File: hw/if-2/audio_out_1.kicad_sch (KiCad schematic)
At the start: 0 parts

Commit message: First draft of schematic
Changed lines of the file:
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@@
 	(text "(Will Be Copy of R1 Audio Output)"
 		(exclude_from_sim no)
-		(at 141.732 90.932 0)
+		(at 146.812 103.124 0)
 		(effects
 			(font

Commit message: First draft of schematic
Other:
- note added: "(Will Be Copy of R0 Audio Output)"
- note removed: "(Will Be Copy of R1 Audio Output)"
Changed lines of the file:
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@@
 		(comment 2 "NOT FOR COMMERCIAL USE")
 	)
-	(text "(Will Be Copy of R1 Audio Output)"
+	(text "(Will Be Copy of R0 Audio Output)"
 		(exclude_from_sim no)
 		(at 146.812 103.124 0)

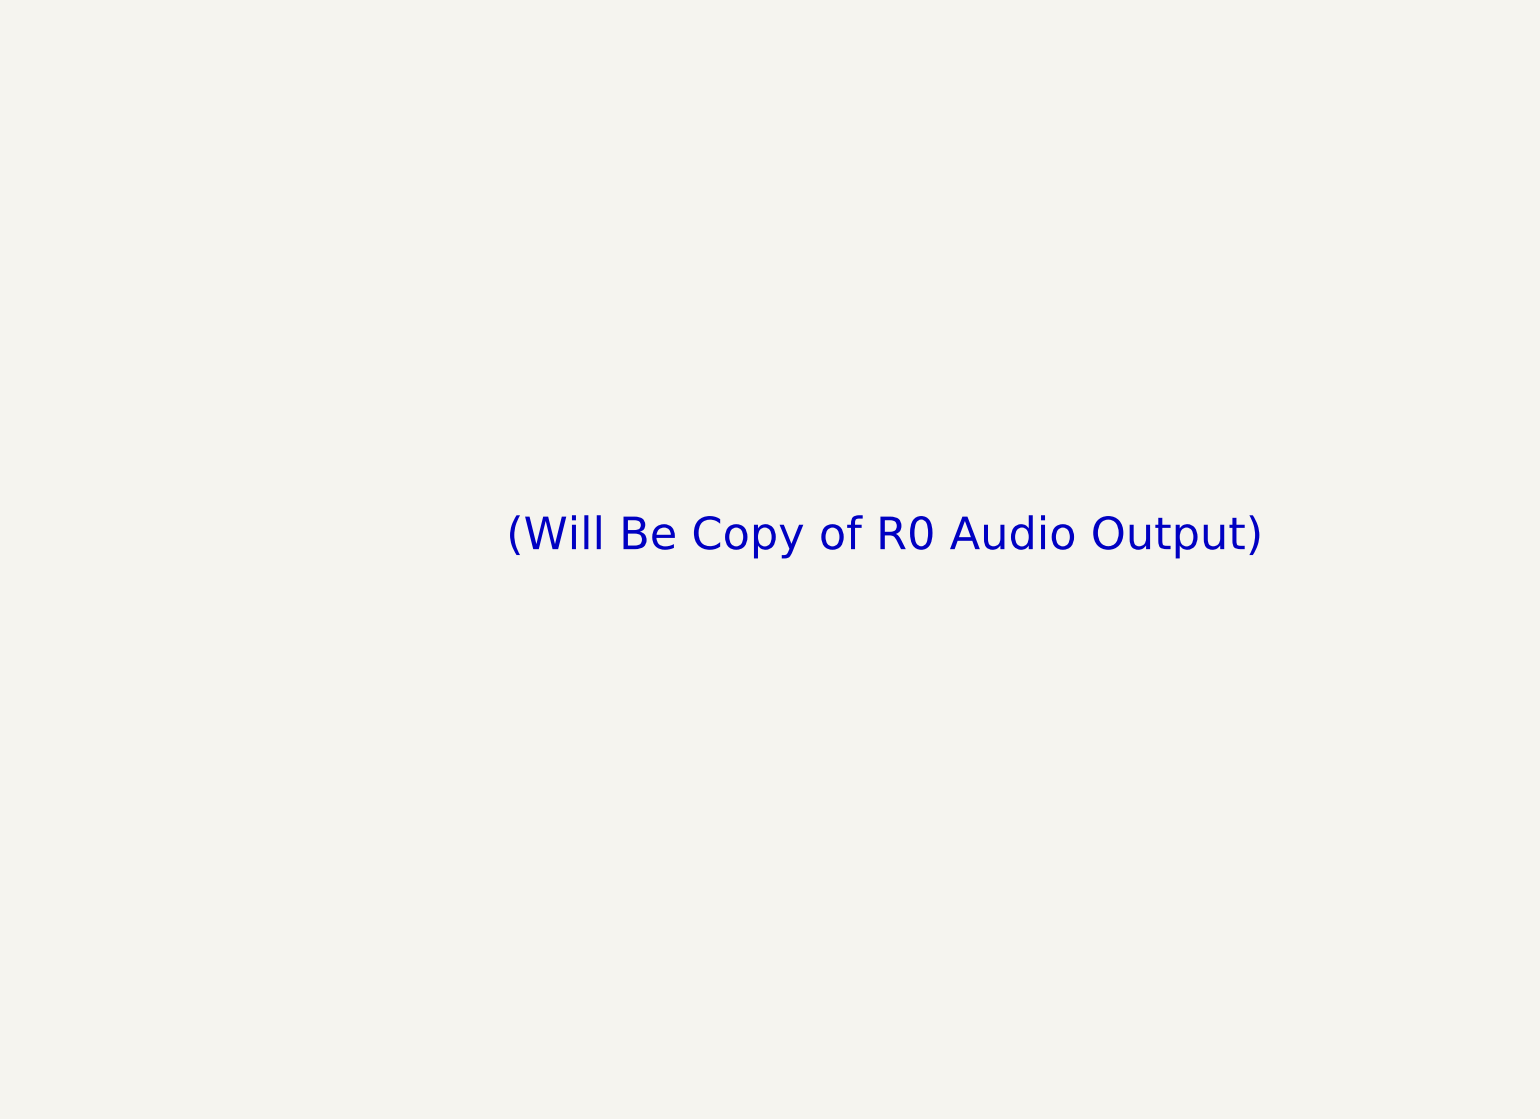
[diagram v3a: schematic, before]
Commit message: Ready to do layout on IF2 board
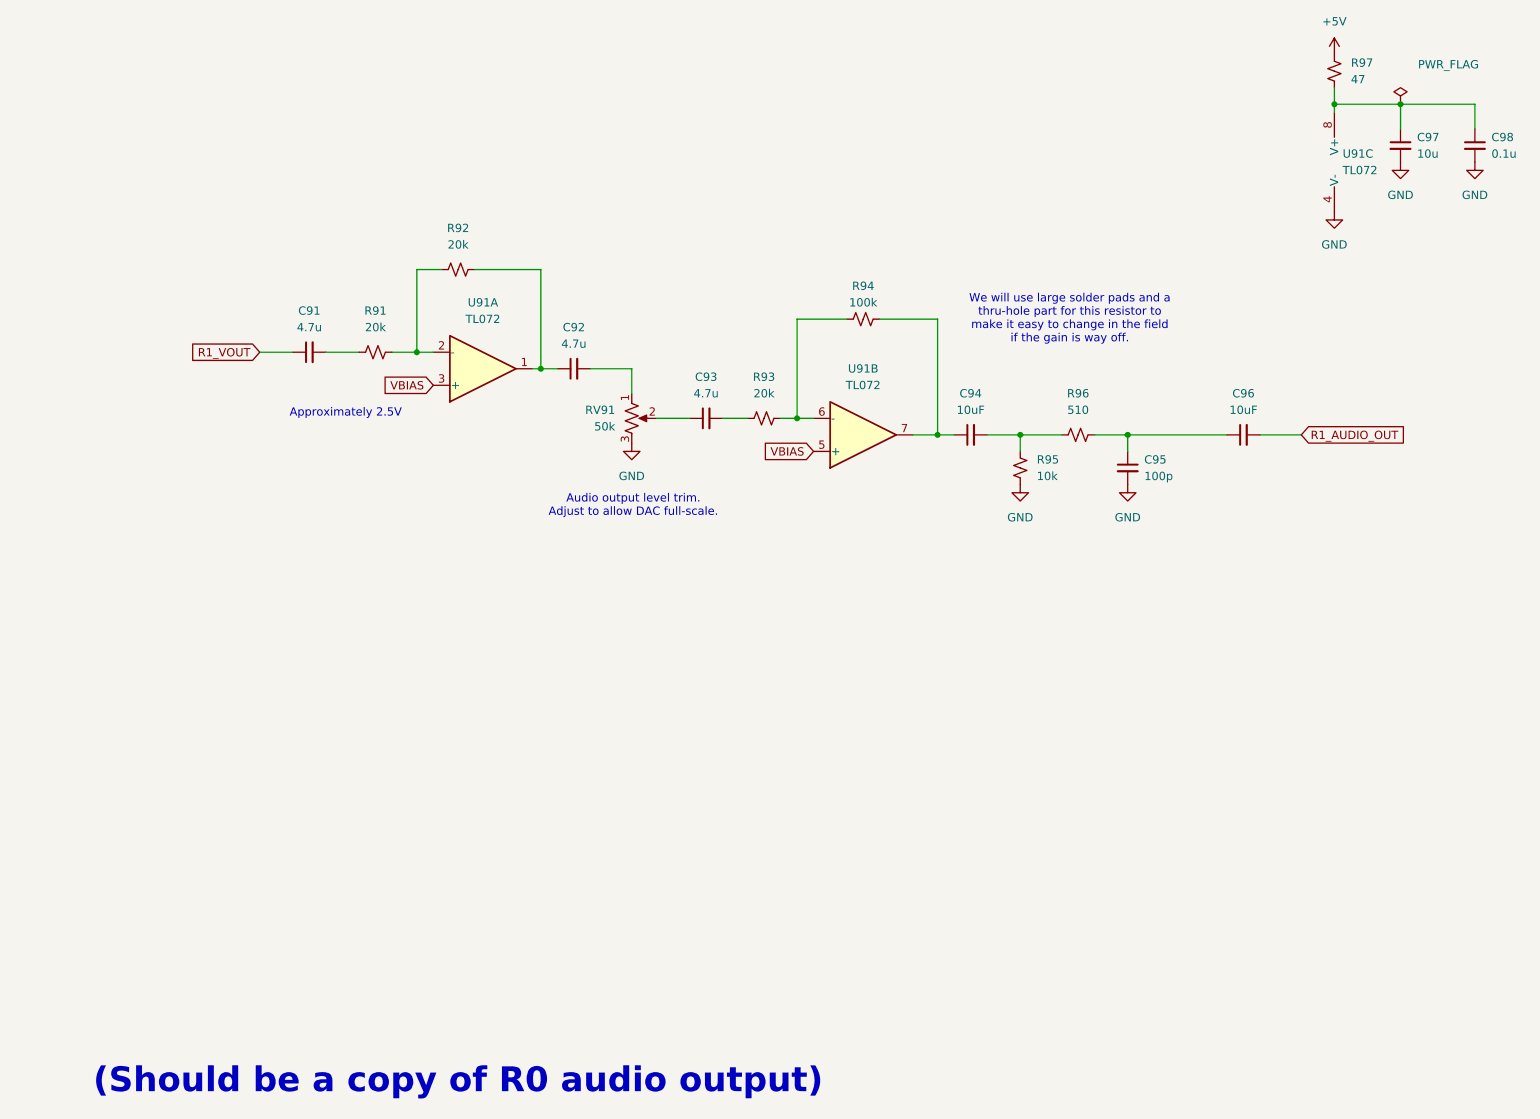
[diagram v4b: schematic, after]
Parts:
- added C91, C92, C93: 4.7u, Capacitor_SMD:C_0805_2012Metric_Pad1.18x1.45mm_HandSolder, symbol Device:C_Small
- added C94, C96: 10uF, Capacitor_SMD:C_0805_2012Metric_Pad1.18x1.45mm_HandSolder, symbol Device:C_Small
- added C95: 100p, Capacitor_SMD:C_0805_2012Metric_Pad1.18x1.45mm_HandSolder, symbol Device:C_Small
- added C97: 10u, Capacitor_SMD:C_0805_2012Metric_Pad1.18x1.45mm_HandSolder, symbol Device:C_Small
- added C98: 0.1u, Capacitor_SMD:C_0805_2012Metric_Pad1.18x1.45mm_HandSolder, symbol Device:C_Small
- added R91, R92, R93: 20k, Resistor_SMD:R_0805_2012Metric_Pad1.20x1.40mm_HandSolder, symbol Device:R_Small_US
- added R94: 100k, Resistor_THT:R_Axial_DIN0516_L15.5mm_D5.0mm_P5.08mm_Vertical, symbol Device:R_Small_US
- added R95: 10k, Resistor_SMD:R_0805_2012Metric_Pad1.20x1.40mm_HandSolder, symbol Device:R_Small_US
- added R96: 510, Resistor_SMD:R_0805_2012Metric_Pad1.20x1.40mm_HandSolder, symbol Device:R_Small_US
- added R97: 47, Resistor_SMD:R_0805_2012Metric_Pad1.20x1.40mm_HandSolder, symbol Device:R_Small_US
- added RV91: 50k, bruce-footprints:POT_3362P, symbol Device:R_Potentiometer_US
- added U91: TL072, Package_SO:SOIC-8_3.9x4.9mm_P1.27mm, symbol Amplifier_Operational:TL072
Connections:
- new net: C97.1, C98.1, R97.1, U91.8 (V+)
- new net: C93.1, RV91.2
- new net: C93.2, R93.1
- new net: R91.2, R92.1, U91.2 (-)
- new net: C92.1, R92.2, U91.1
- new net: C95.1, C96.1, R96.2
- new net: C91.2, R91.1
- new net: R93.2, R94.1, U91.6 (-)
- new net: C92.2, RV91.1
- new net: C94.1, R94.2, U91.7
- new net: C94.2, R95.1, R96.1
- new net +5V: R97.2
- new net GND: C95.2, C97.2, C98.2, R95.2, RV91.3, U91.4 (V-)
- new net R1_AUDIO_OUT: C96.2
- new net R1_VOUT: C91.1
- new net VBIAS: U91.3 (+), U91.5 (+)
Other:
- note added: "(Should be a copy of R0 audio output)"
- note added: "Approximately 2.5V"
- note added: "Audio output level trim. Adjust to allow DAC full-scale."
- note added: "We will use large solder pads and a thru-hole part for this resistor to make it easy to change in the field if the gain is way off."
- note removed: "(Will Be Copy of R0 Audio Output)"
- title: Audio Output Processing (Radio 0) -> COS/CTCSS/PTT Controls (Radio 1)

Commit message: Making progress on layout
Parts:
- added TP7: TestPoint, TestPoint:TestPoint_Pad_2.5x2.5mm, symbol Connector:TestPoint
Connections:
- net R1_VOUT: now also TP7.1
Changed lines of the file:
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@@
+	)
+	(junction
+		(at 54.61 74.93)
+		(diameter 0)
+		(color 0 0 0 0)
 	)
 	(junction
@@
 	(wire
 		(pts
+			(xy 54.61 74.93) (xy 55.88 74.93)
+		)
+		(stroke
+			(width 0)
+			(type default)
+		)
+	)
+	(wire
+		(pts
 			(xy 237.49 40.64) (xy 237.49 36.83)
 		)
@@
 	(wire
 		(pts
+			(xy 54.61 67.31) (xy 54.61 74.93)
+		)
+		(stroke
+			(width 0)
+			(type default)
+		)
+	)
+	(wire
+		(pts
 			(xy 71.12 74.93) (xy 74.93 74.93)
 		)
@@
 	(wire
 		(pts
-			(xy 50.8 74.93) (xy 55.88 74.93)
+			(xy 50.8 74.93) (xy 54.61 74.93)
 		)
 		(stroke
@@
 				)
 			)
+		)
+	)
+	(symbol
+		(lib_id "Connector:TestPoint")
+		(at 54.61 67.31 0)
+		(unit 1)
+		(exclude_from_sim no)
+		(in_bom yes)
+		(on_board yes)
+		(dnp no)
+		(fields_autoplaced yes)
+		(property "Reference" "TP7"
+			(at 57.15 62.7379 0)
+			(effects
+				(font
+					(size 1.27 1.27)
+				)
+				(justify left)
+			)
+		)
+		(property "Value" "TestPoint"
+			(at 57.15 65.2779 0)
+			(effects
+				(font
+					(size 1.27 1.27)
+				)
+				(justify left)
+			)
+		)
+		(property "Footprint" "TestPoint:TestPoint_Pad_2.5x2.5mm"
+			(at 59.69 67.31 0)
+			(effects
+				(font
+					(size 1.27 1.27)
+				)
+				(hide yes)
+			)
+		)
+		(property "Datasheet" "~"
+			(at 59.69 67.31 0)
+			(effects
+				(font
+					(size 1.27 1.27)
+				)
+				(hide yes)
+			)
+		)
+		(property "Description" "test point"
+			(at 54.61 67.31 0)
+			(effects
+				(font
+					(size 1.27 1.27)
+				)
+				(hide yes)
+			)
+		)
+		(pin "1"
+		)
+		(instances
+			(project "if-2"
+				(path "/a8c2d6aa-29bb-49bd-a367-0d62a0a32480/34b2b7e3-3a7b-4c6a-8d8d-e895b4fba2b7"
+					(reference "TP7")
+					(unit 1)
+				)
+			)
